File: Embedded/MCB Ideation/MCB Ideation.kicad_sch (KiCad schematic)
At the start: 18 parts, among them J1 MSD-1-A, U1 ICM-20948, U2 BME280, U3 USB

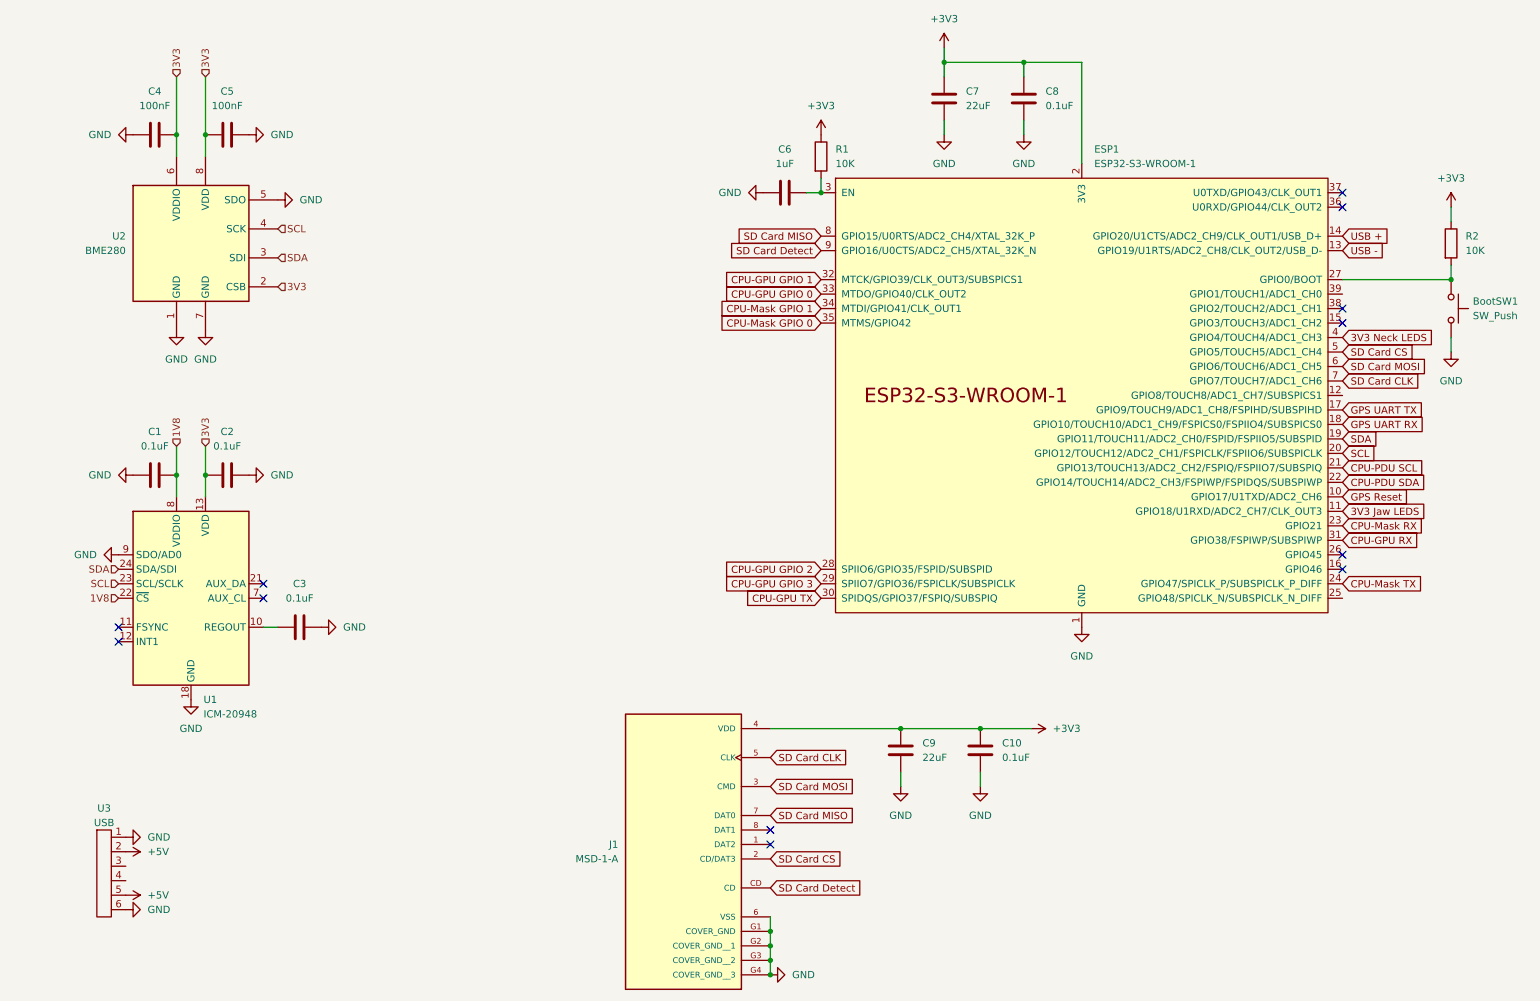
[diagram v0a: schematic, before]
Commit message: Ideation PCB Component Compaction
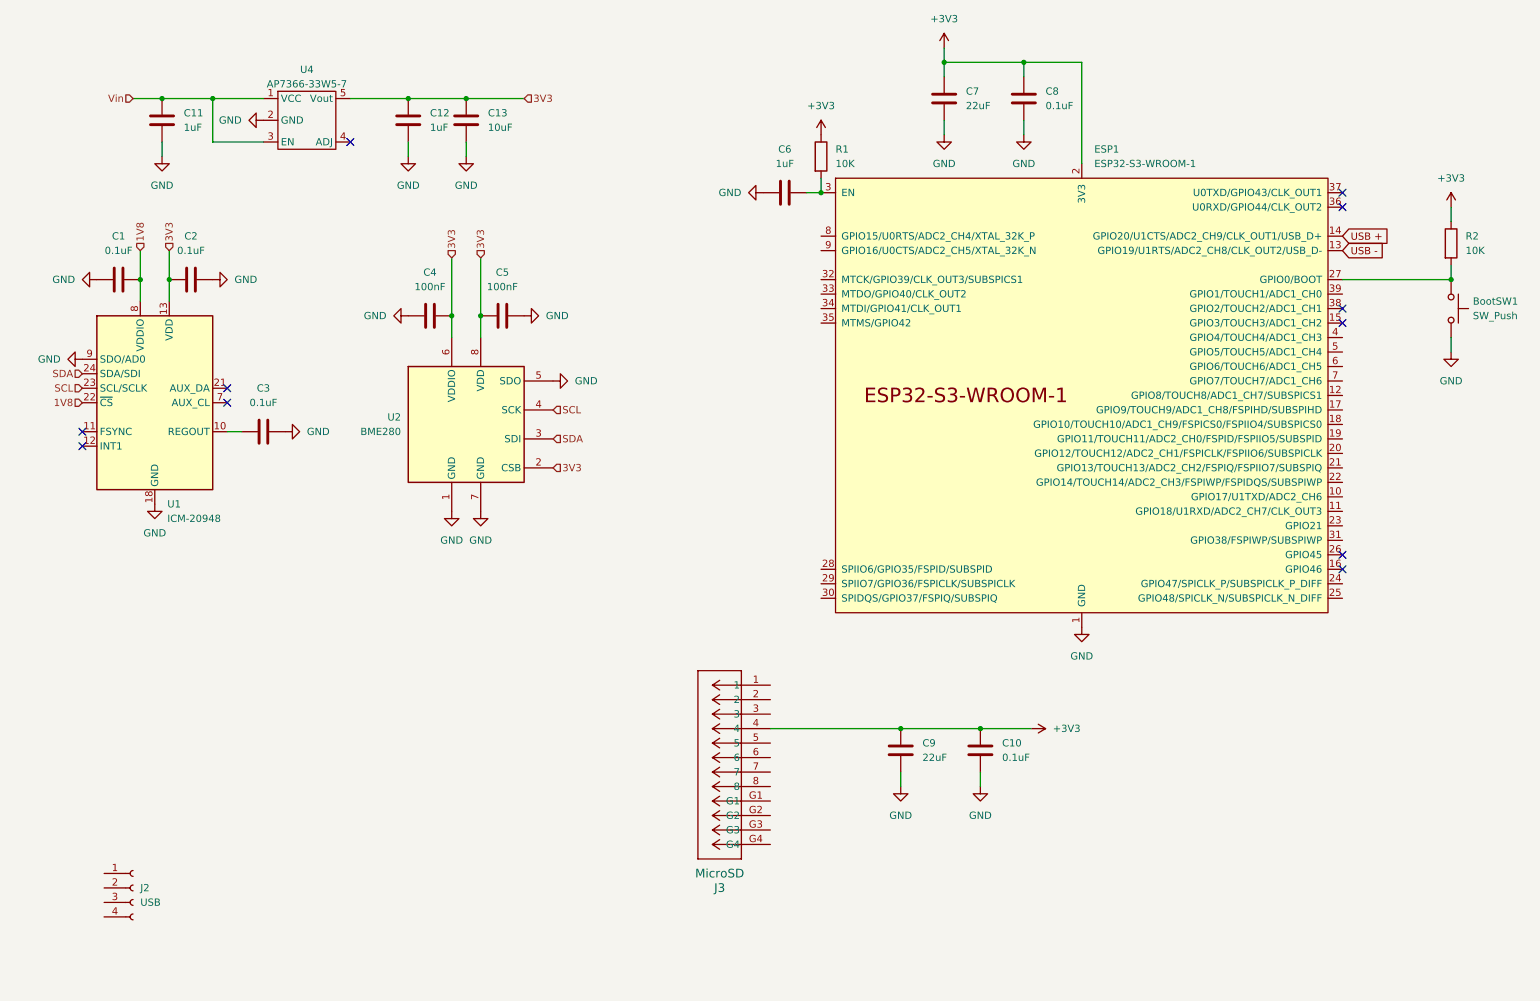
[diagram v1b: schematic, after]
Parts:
- removed J1: MSD-1-A, MicroSD_MSD_1_A:CUI_MSD-1-A, symbol MicroSD_MSD_1_A:MSD-1-A
- removed U3: USB, FFC_Connector:FFC Aliexpress 0.5mm 6P, symbol FCC_Connector:FFC_6P
- added C11, C12: 1uF, Resistor_SMD:R_0603_1608Metric, symbol Device:C
- added C13: 10uF, Capacitor_SMD:C_0603_1608Metric, symbol Device:C
- added J2: USB, Connector_PinSocket_1.27mm:PinSocket_1x04_P1.27mm_Vertical, symbol Connector:Conn_01x04_Socket
- added J3: MicroSD, MicroSD_473092651:CONN12_47309-2651_MOL, symbol MicroSD_473092651:473092651
- added U4: AP7366-33W5-7, AP7366-SOT25:AP7366, symbol AP7366_SOT_25:AP7366_SOT25
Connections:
- net +3V3: now also J3.4
- net 3V3: now also C12.1, C13.1, U4.5 (Vout)
- net GND: now also C11.2, C12.2, C13.2, U4.2 (GND)
- net SCL: no longer ESP1.20 (GPIO12/TOUCH12/ADC2_CH1/FSPICLK/FSPIIO6/SUBSPICLK)
- net SDA: no longer ESP1.19 (GPIO11/TOUCH11/ADC2_CH0/FSPID/FSPIIO5/SUBSPID)
- net 3V3 Jaw LEDS: no longer names the net of ESP1.11 (GPIO18/U1RXD/ADC2_CH7/CLK_OUT3)
- net 3V3 Neck LEDS: no longer names the net of ESP1.4 (GPIO4/TOUCH4/ADC1_CH3)
- net CPU-GPU GPIO 0: no longer names the net of ESP1.33 (MTDO/GPIO40/CLK_OUT2)
- net CPU-GPU GPIO 1: no longer names the net of ESP1.32 (MTCK/GPIO39/CLK_OUT3/SUBSPICS1)
- net CPU-GPU GPIO 2: no longer names the net of ESP1.28 (SPIIO6/GPIO35/FSPID/SUBSPID)
- net CPU-GPU GPIO 3: no longer names the net of ESP1.29 (SPIIO7/GPIO36/FSPICLK/SUBSPICLK)
- net CPU-GPU RX: no longer names the net of ESP1.31 (GPIO38/FSPIWP/SUBSPIWP)
- net CPU-GPU TX: no longer names the net of ESP1.30 (SPIDQS/GPIO37/FSPIQ/SUBSPIQ)
- net CPU-Mask GPIO 0: no longer names the net of ESP1.35 (MTMS/GPIO42)
- net CPU-Mask GPIO 1: no longer names the net of ESP1.34 (MTDI/GPIO41/CLK_OUT1)
- net CPU-Mask RX: no longer names the net of ESP1.23 (GPIO21)
- net CPU-Mask TX: no longer names the net of ESP1.24 (GPIO47/SPICLK_P/SUBSPICLK_P_DIFF)
- net CPU-PDU SCL: no longer names the net of ESP1.21 (GPIO13/TOUCH13/ADC2_CH2/FSPIQ/FSPIIO7/SUBSPIQ)
- net CPU-PDU SDA: no longer names the net of ESP1.22 (GPIO14/TOUCH14/ADC2_CH3/FSPIWP/FSPIDQS/SUBSPIWP)
- net GPS Reset: no longer names the net of ESP1.10 (GPIO17/U1TXD/ADC2_CH6)
- net GPS UART RX: no longer names the net of ESP1.18 (GPIO10/TOUCH10/ADC1_CH9/FSPICS0/FSPIIO4/SUBSPICS0)
- net GPS UART TX: no longer names the net of ESP1.17 (GPIO9/TOUCH9/ADC1_CH8/FSPIHD/SUBSPIHD)
- net SD Card CLK: no longer names the net of ESP1.7 (GPIO7/TOUCH7/ADC1_CH6)
- net SD Card CS: no longer names the net of ESP1.5 (GPIO5/TOUCH5/ADC1_CH4)
- net SD Card Detect: no longer names the net of ESP1.9 (GPIO16/U0CTS/ADC2_CH5/XTAL_32K_N)
- net SD Card MISO: no longer names the net of ESP1.8 (GPIO15/U0RTS/ADC2_CH4/XTAL_32K_P)
- net SD Card MOSI: no longer names the net of ESP1.6 (GPIO6/TOUCH6/ADC1_CH5)
- new net Vin: C11.1, U4.1 (VCC), U4.3 (EN)
- no-connect marks 12 -> 11
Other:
- moved on the sheet: C1, C2, C3, C4, C5, U1, U2

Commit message: Feature Listing & Organisation
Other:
- note added: "HUB75 Combined Pins"
- note added: "HUB75 Display 0"
- note added: "HUB75 Display 1"

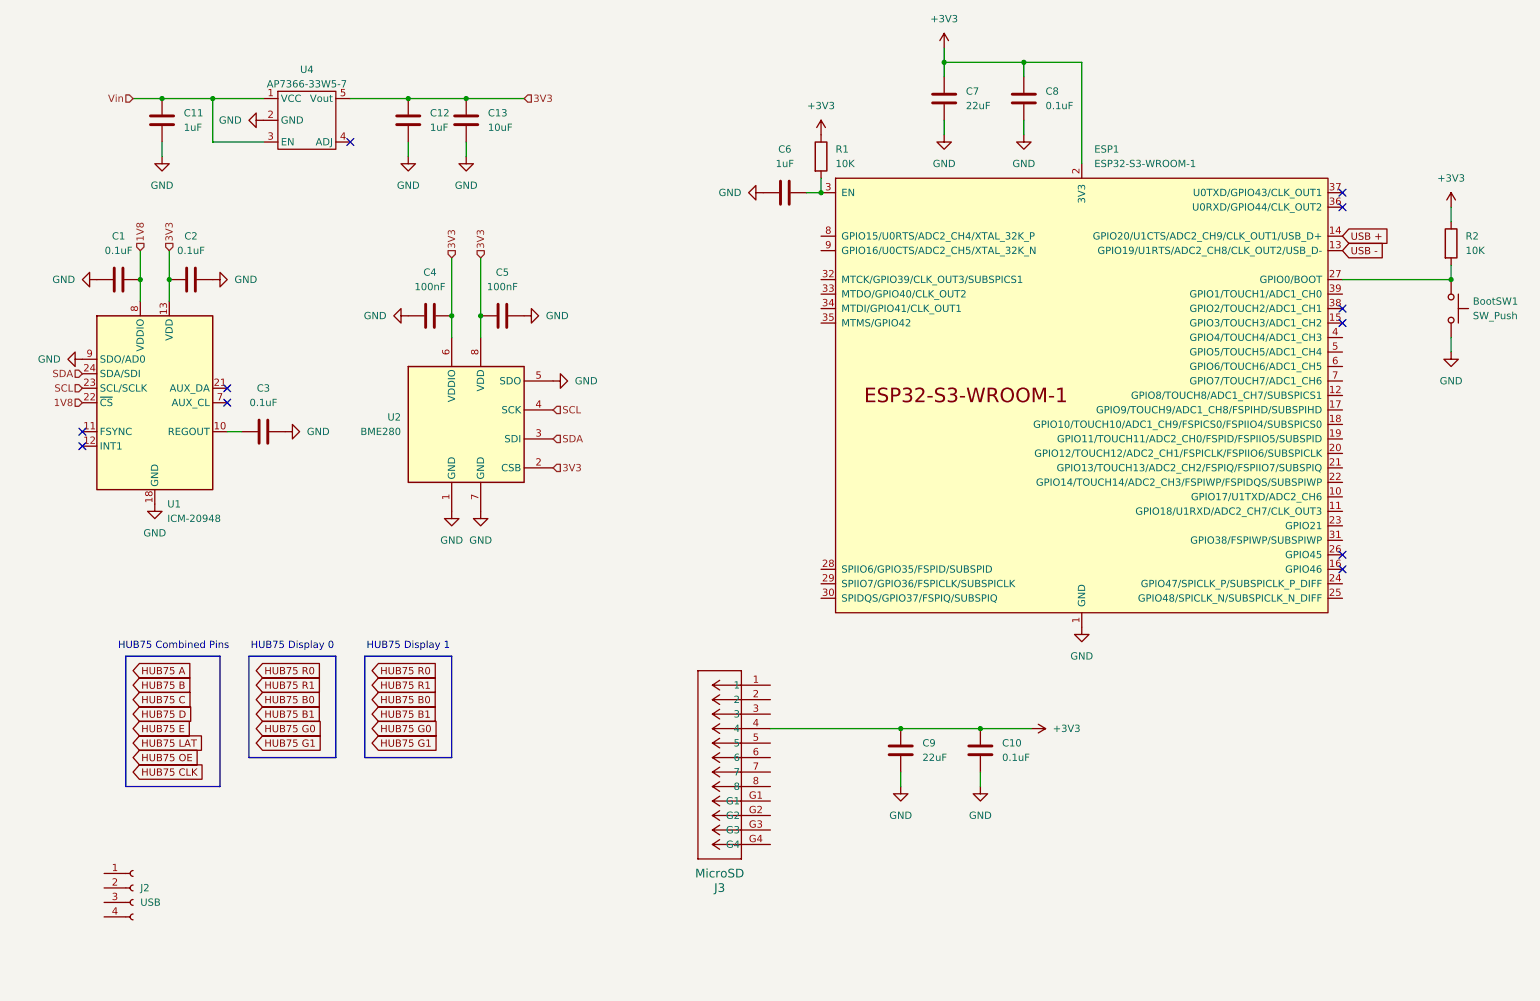
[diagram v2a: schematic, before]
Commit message: Added Sensored
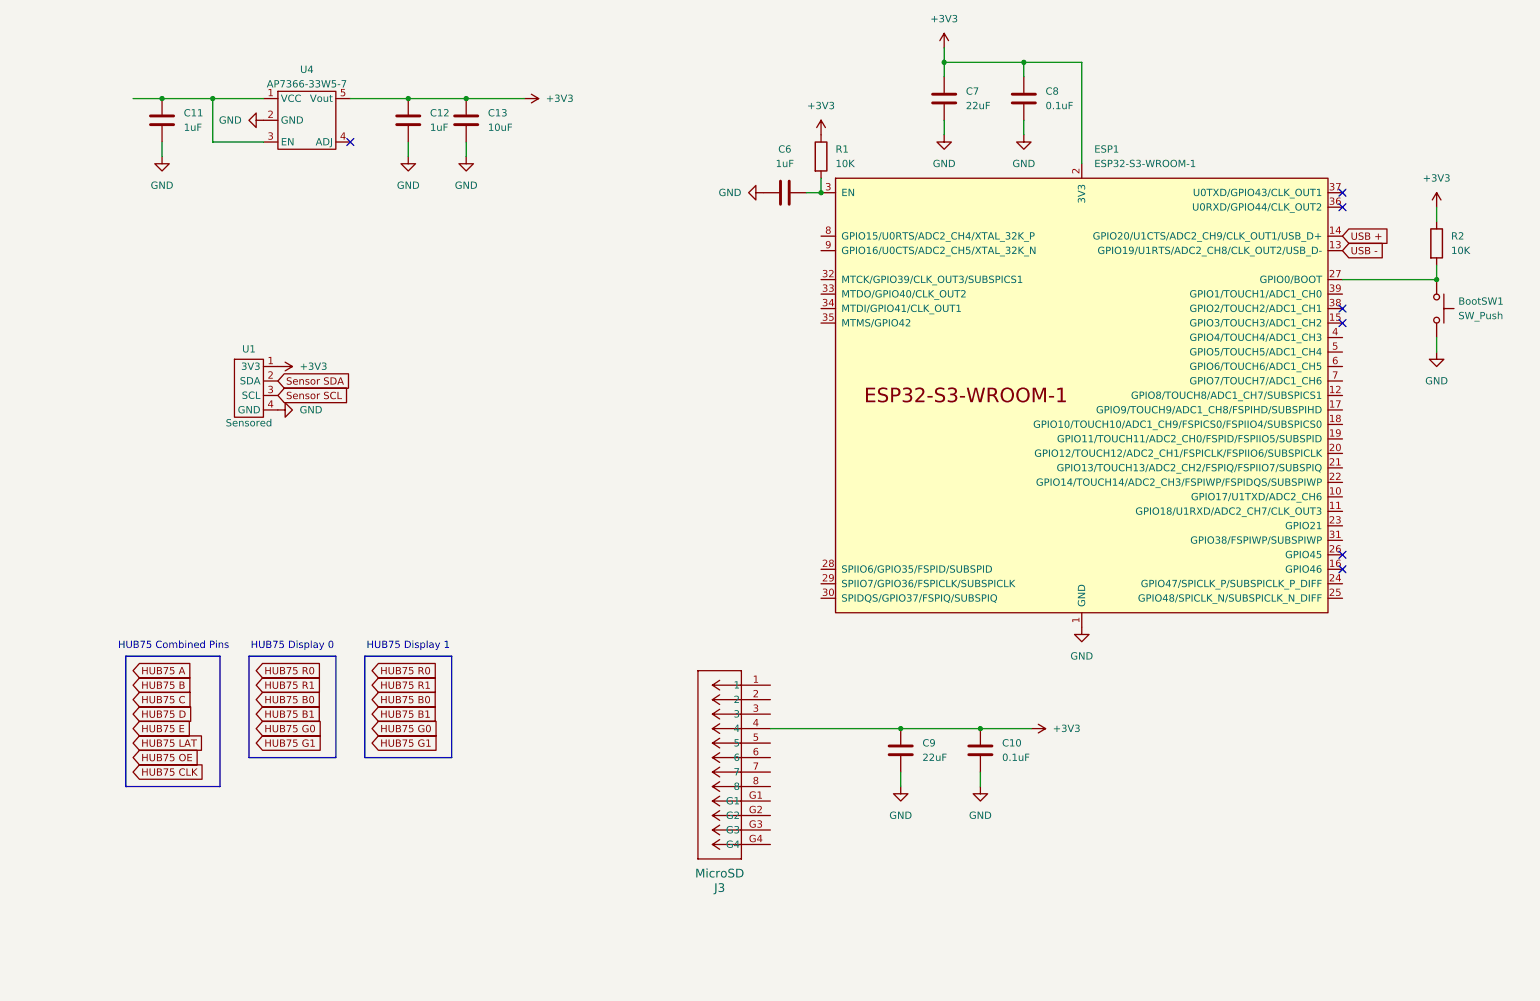
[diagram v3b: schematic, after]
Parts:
- removed C1, C2, C3: 0.1uF, Capacitor_SMD:C_0402_1005Metric_Pad0.74x0.62mm_HandSolder, symbol Device:C
- removed C4, C5: 100nF, Capacitor_SMD:C_0402_1005Metric_Pad0.74x0.62mm_HandSolder, symbol Device:C
- removed J2: USB, Connector_PinSocket_1.27mm:PinSocket_1x04_P1.27mm_Vertical, symbol Connector:Conn_01x04_Socket
- removed U1: ICM-20948, Sensor_Motion:InvenSense_QFN-24_3x3mm_P0.4mm, symbol Sensor_Motion:ICM-20948
- removed U2: BME280, Package_LGA:Bosch_LGA-8_2.5x2.5mm_P0.65mm_ClockwisePinNumbering, symbol Sensor:BME280
- added U1: Sensored, Sensored:Sensored, symbol Sensored:Sensored
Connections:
- net 3V3 is gone; now on net +3V3: C12.1, C13.1, U4.5 (Vout)
- net +3V3: now also U1.1 (3V3)
- net GND: now also U1.4 (GND)
- net Vin: no longer names the net of C11.1, U4.1 (VCC), U4.3 (EN)
- new net Sensor SCL: U1.3 (SCL)
- new net Sensor SDA: U1.2 (SDA)
- no-connect marks 11 -> 7
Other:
- moved on the sheet: BootSW1, R2

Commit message: Added Expansion Pins
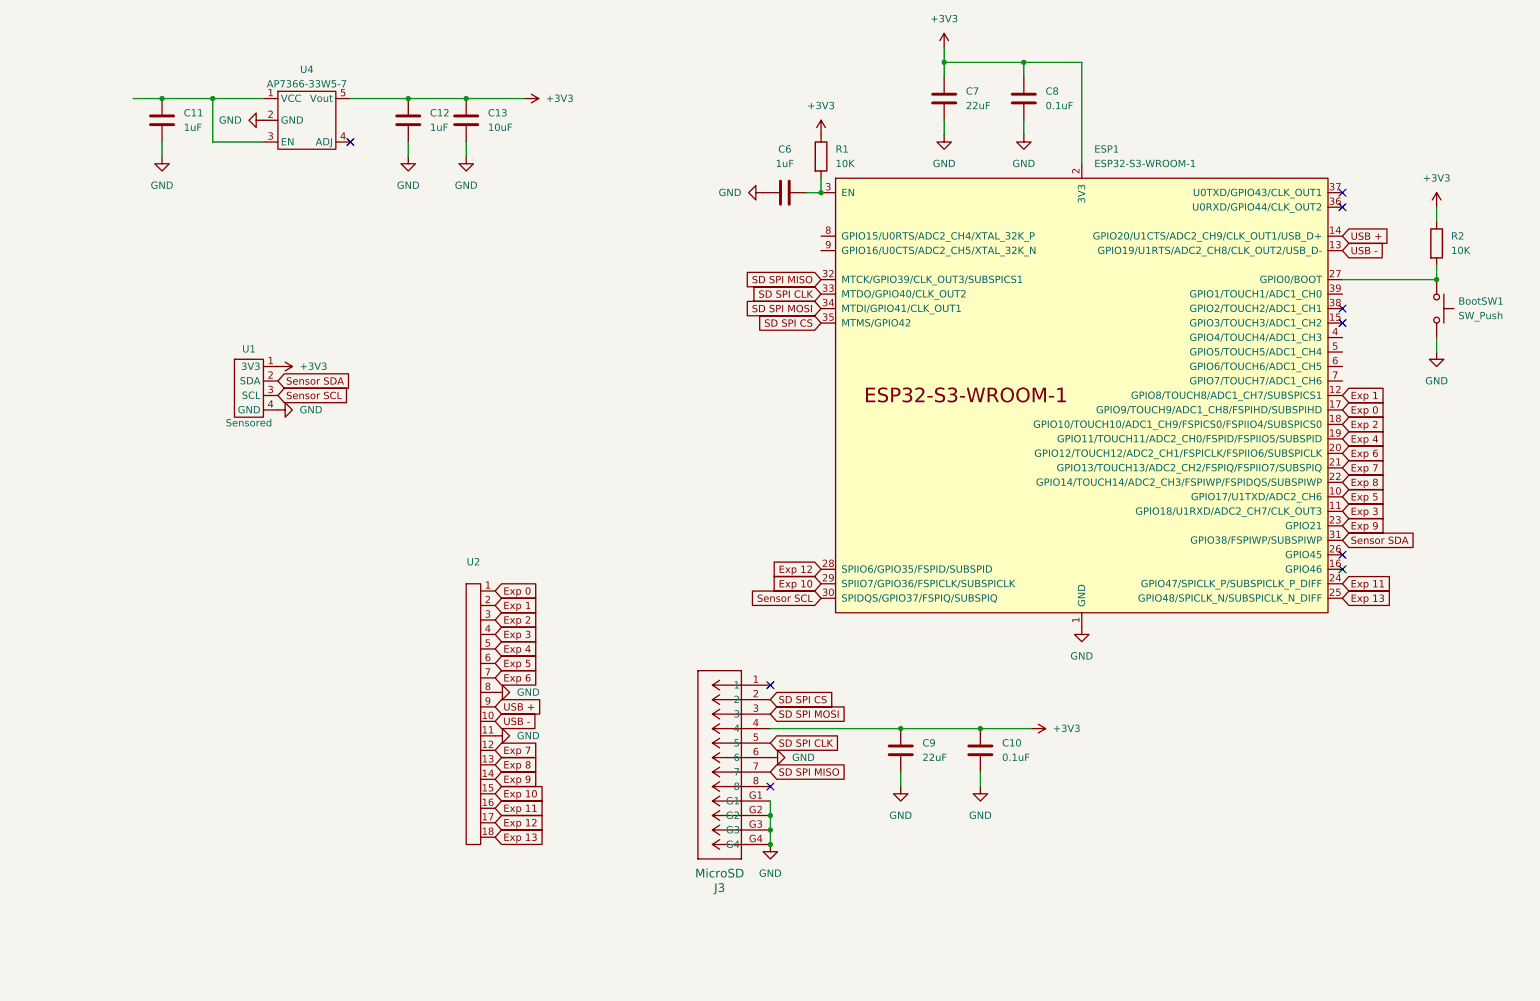
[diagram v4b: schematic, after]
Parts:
- added U2: ~, FFC_Connector:FFC Aliexpress 0.5mm 18P, symbol FCC_Connector:FFC_18P
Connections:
- net GND: now also J3.6, J3.G1, J3.G2, J3.G3, J3.G4, U2.11, U2.8
- net Sensor SCL: now also ESP1.30 (SPIDQS/GPIO37/FSPIQ/SUBSPIQ)
- net Sensor SDA: now also ESP1.31 (GPIO38/FSPIWP/SUBSPIWP)
- net USB +: now also U2.9
- net USB -: now also U2.10
- net Exp 5: now reaches ESP1.10 (GPIO17/U1TXD/ADC2_CH6)
- net Exp 5: now also U2.6
- net Exp 3: now reaches ESP1.11 (GPIO18/U1RXD/ADC2_CH7/CLK_OUT3)
- net Exp 3: now also U2.4
- net Exp 1: now reaches ESP1.12 (GPIO8/TOUCH8/ADC1_CH7/SUBSPICS1)
- net Exp 1: now also U2.2
- net Exp 0: now reaches ESP1.17 (GPIO9/TOUCH9/ADC1_CH8/FSPIHD/SUBSPIHD)
- net Exp 0: now also U2.1
- net Exp 2: now reaches ESP1.18 (GPIO10/TOUCH10/ADC1_CH9/FSPICS0/FSPIIO4/SUBSPICS0)
- net Exp 2: now also U2.3
- net Exp 4: now reaches ESP1.19 (GPIO11/TOUCH11/ADC2_CH0/FSPID/FSPIIO5/SUBSPID)
- net Exp 4: now also U2.5
- net Exp 6: now reaches ESP1.20 (GPIO12/TOUCH12/ADC2_CH1/FSPICLK/FSPIIO6/SUBSPICLK)
- net Exp 6: now also U2.7
- net Exp 7: now reaches ESP1.21 (GPIO13/TOUCH13/ADC2_CH2/FSPIQ/FSPIIO7/SUBSPIQ)
- net Exp 7: now also U2.12
- net Exp 8: now reaches ESP1.22 (GPIO14/TOUCH14/ADC2_CH3/FSPIWP/FSPIDQS/SUBSPIWP)
- net Exp 8: now also U2.13
- net Exp 9: now reaches ESP1.23 (GPIO21)
- net Exp 9: now also U2.14
- net Exp 11: now reaches ESP1.24 (GPIO47/SPICLK_P/SUBSPICLK_P_DIFF)
- net Exp 11: now also U2.16
- net Exp 13: now reaches ESP1.25 (GPIO48/SPICLK_N/SUBSPICLK_N_DIFF)
- net Exp 13: now also U2.18
- net Exp 12: now reaches ESP1.28 (SPIIO6/GPIO35/FSPID/SUBSPID)
- net Exp 12: now also U2.17
- net Exp 10: now reaches ESP1.29 (SPIIO7/GPIO36/FSPICLK/SUBSPICLK)
- net Exp 10: now also U2.15
- net SD SPI MISO: now reaches ESP1.32 (MTCK/GPIO39/CLK_OUT3/SUBSPICS1)
- net SD SPI MISO: now also J3.7
- net SD SPI CLK: now reaches ESP1.33 (MTDO/GPIO40/CLK_OUT2)
- net SD SPI CLK: now also J3.5
- net SD SPI MOSI: now reaches ESP1.34 (MTDI/GPIO41/CLK_OUT1)
- net SD SPI MOSI: now also J3.3
- net SD SPI CS: now reaches ESP1.35 (MTMS/GPIO42)
- net SD SPI CS: now also J3.2
- no-connect marks 7 -> 9
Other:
- note removed: "HUB75 Combined Pins"
- note removed: "HUB75 Display 0"
- note removed: "HUB75 Display 1"
